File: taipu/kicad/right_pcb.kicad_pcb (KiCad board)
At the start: 2 copper layers, 162.9 x 92.4 mm, 56 parts

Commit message: routing
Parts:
- moved S21 8.96 mm to (276.0, 109.0)
- moved S13 8.96 mm to (312.0, 121.0)
- moved S4 8.96 mm to (367.8, 132.4)
- moved S12 8.96 mm to (330.0, 89.5)
- moved S15 8.96 mm to (312.0, 87.0)
- moved _5 8.96 mm to (265.9, 153.6)
- moved D24 8.96 mm to (258.1, 158.1)
- moved S11 8.96 mm to (330.0, 106.5)
- moved MCU1 8.96 mm to (253.0, 107.0)
- moved D8 8.96 mm to (349.7, 117.8)
- moved D17 8.96 mm to (294.0, 128.5)
- moved S24 8.96 mm to (255.6, 153.7)
- moved S17 8.96 mm to (294.0, 123.5)
- moved D14 8.96 mm to (312.0, 109.0)
- moved S1 8.96 mm to (385.7, 134.9)
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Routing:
- net P020: track 0.00 -> 229.8 mm
- net P017: track 0.00 -> 212.2 mm
- net P022: track 0.00 -> 207.4 mm
- net P024: track 0.00 -> 200.8 mm
- net P002: track 0.00 -> 178.0 mm
- net P100: track 0.00 -> 177.2 mm
- net P031: track 0.00 -> 168.7 mm
- net P029: track 0.00 -> 166.4 mm
- net GND: track 0.00 -> 137.8 mm
- net pos: track 0.00 -> 130.0 mm
- net P011: track 0.00 -> 114.4 mm
- net P104: track 0.00 -> 113.9 mm, vias 0 -> 1
- net P115: track 0.00 -> 96.3 mm
- net RAW: track 0.00 -> 45.8 mm
- net mirror_pinky_home: track 0.00 -> 14.9 mm
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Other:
- net class Default removed

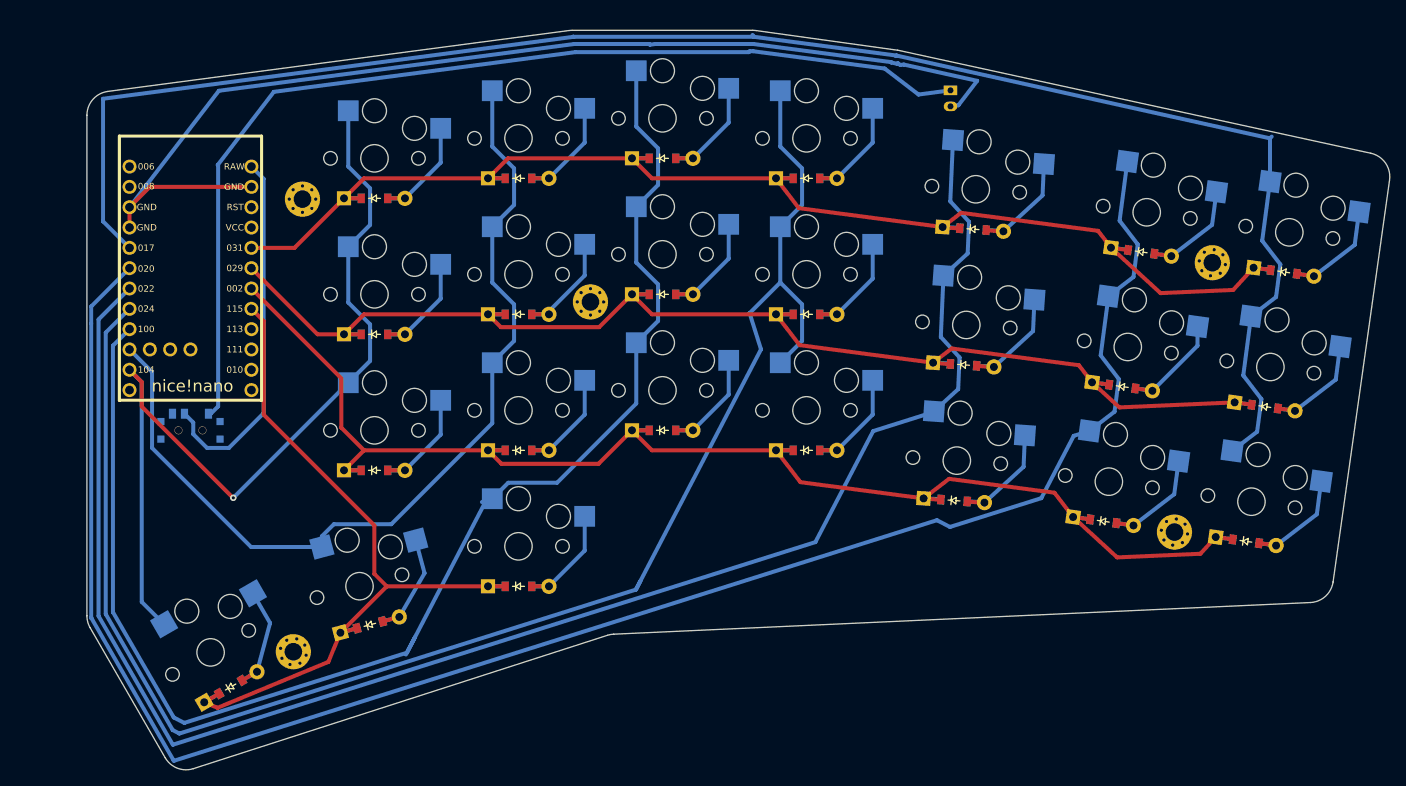
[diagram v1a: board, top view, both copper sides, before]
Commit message: better batery placement
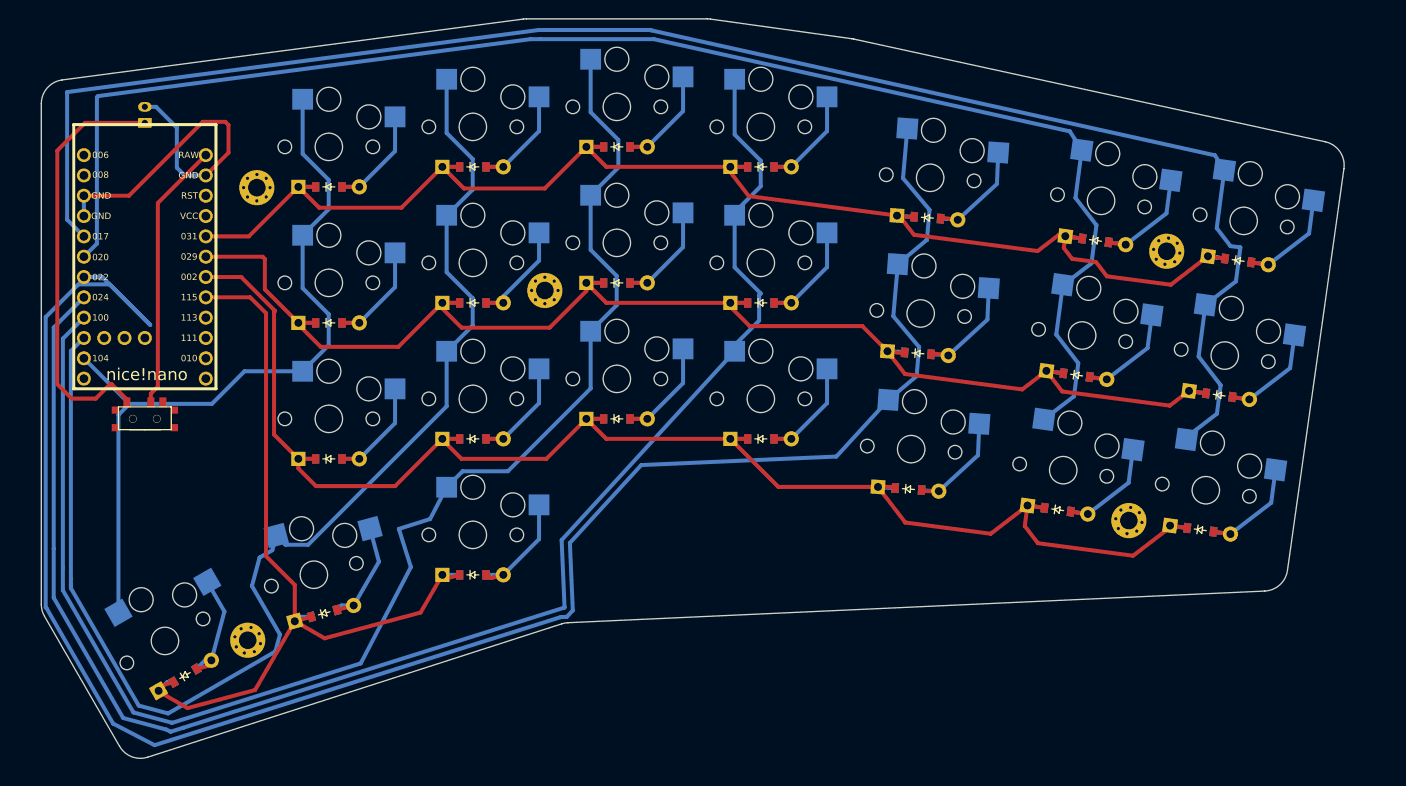
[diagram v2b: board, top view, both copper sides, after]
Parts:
- moved JST1 100.7 mm to (247.3, 86.5), turned to 90 degrees
- moved S21 5.88 mm to (270.3, 107.5)
- moved S12 5.88 mm to (324.3, 88.0)
- moved D24 5.88 mm to (252.4, 156.6)
- moved S13 5.88 mm to (306.3, 119.5)
- moved _2 5.88 mm to (261.3, 95.6)
- moved MCU1 5.88 mm to (247.3, 105.5)
- moved S4 5.88 mm to (362.1, 130.9)
- moved S11 5.88 mm to (324.3, 105.0)
- moved D8 5.88 mm to (344.0, 116.3)
- moved D17 5.88 mm to (288.3, 127.0)
- moved D14 5.88 mm to (306.3, 107.5)
- moved S1 5.88 mm to (380.0, 133.4)
- moved D23 5.88 mm to (269.8, 148.8)
- moved D2 5.88 mm to (381.6, 121.6)
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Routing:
- net GND: track 137.8 -> 46.2 mm
- net pos: track 130.0 -> 52.9 mm
- net P011: track 114.4 -> 160.1 mm
- net P020: track 229.8 -> 186.1 mm
- net P022: track 207.4 -> 237.1 mm
- net P104: track 113.9 -> 97.5 mm, vias 1 -> 0
- net RAW: track 45.8 -> 33.7 mm
- net P002: track 178.0 -> 189.8 mm
- net P115: track 96.3 -> 107.0 mm
- net P029: track 166.4 -> 175.3 mm
- net P031: track 168.7 -> 176.1 mm
- net P024: track 200.8 -> 194.1 mm
- net P017: track 212.2 -> 207.0 mm
- net P100: track 177.2 -> 179.5 mm
- net mirror_clone_outer_top: track 14.9 -> 16.0 mm

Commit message: add logo
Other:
- board text added: "タイプ"
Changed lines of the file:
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@@
 			(outputformat 1)
 			(mirror no)
-			(drillshape 1)
+			(drillshape 0)
 			(scaleselection 1)
-			(outputdirectory "")
+			(outputdirectory "right_gerbers/")
 		)
 	)
@@
 		(layer "Edge.Cuts")
 	)
+	(gr_text "タイプ"
+		(at 297.6 148 2.5)
+		(layer "F.SilkS")
+		(effects
+			(font
+				(size 11 11)
+				(thickness 1.375)
+			)
+			(justify left bottom)
+		)
+	)
 	(segment
